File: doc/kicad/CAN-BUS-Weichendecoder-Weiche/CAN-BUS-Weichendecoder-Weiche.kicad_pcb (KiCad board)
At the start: 2 copper layers, 109.2 x 81.3 mm, 43 parts, among them J1 250-1404, J2 250-1404, J22 CAN-BUS, J23 CAN-BUS, J3 250-1404, J4 250-1404, J5 250-1404, J6 GND 12V DC +, J7 DCC IN, J8 I²C D C + -, U1 6N136, U2 Arduino_Nano, U3 ULN2803A, U4 ULN2803A, U5 TSR_1-2450

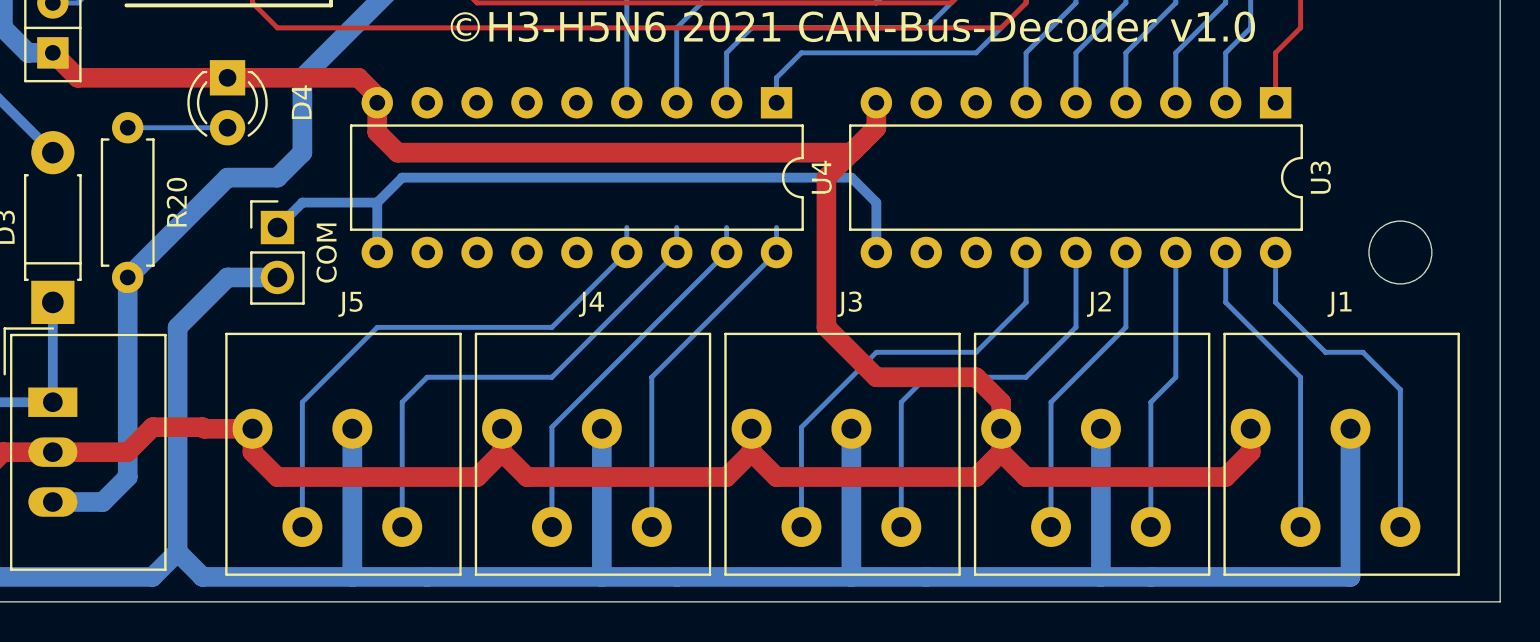
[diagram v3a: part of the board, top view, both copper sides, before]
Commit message: Buchen zu den Weichen gedreht, damit sie besser auf das Board passsen
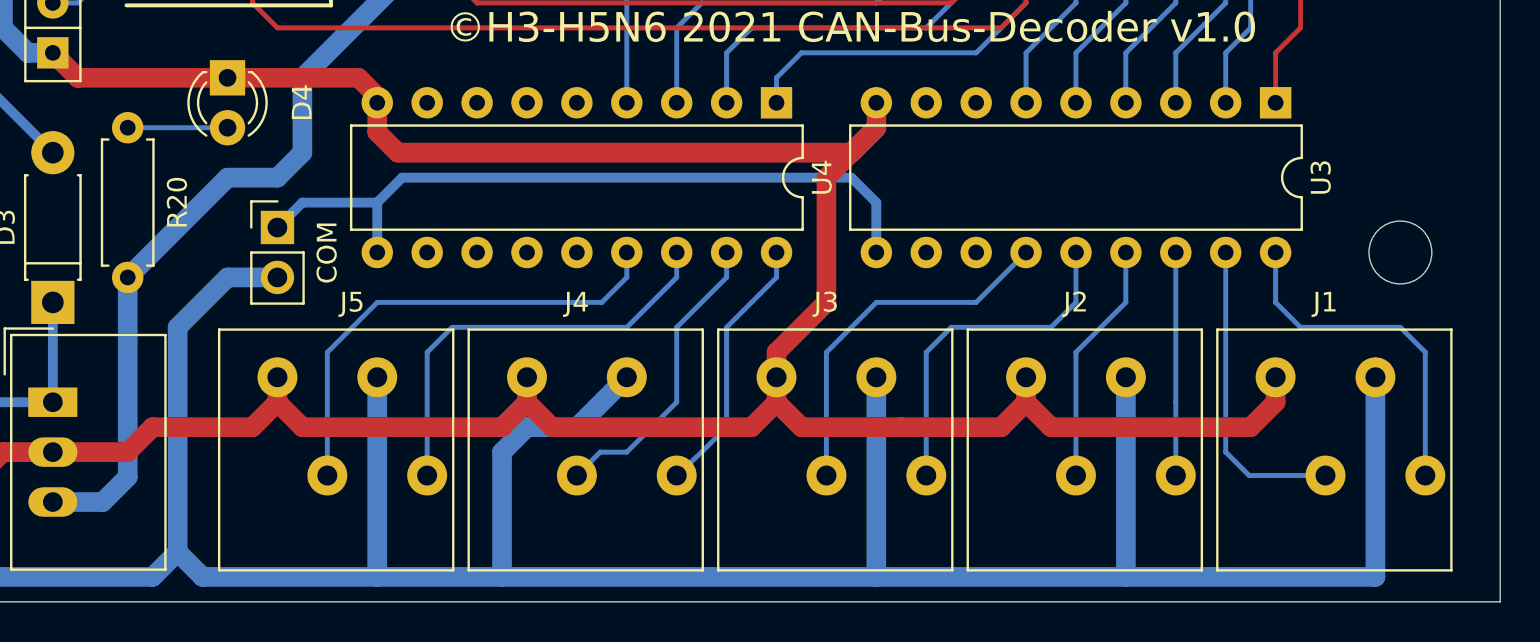
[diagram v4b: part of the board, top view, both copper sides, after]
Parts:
- moved J1 9.92 mm to (154.9, 91.4), turned to 0 degrees
- moved J2 9.92 mm to (142.2, 91.4), turned to 0 degrees
- moved J3 9.92 mm to (129.5, 91.4), turned to 0 degrees
- moved J4 9.92 mm to (116.8, 91.4), turned to 0 degrees
- moved J5 9.92 mm to (104.1, 91.4), turned to 0 degrees
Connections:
- J1 pad 1: Net-(J1-Pad1) -> GND
- J1 pad 2: +12V -> Net-(J1-Pad2)
- J1 pad 3: Net-(J1-Pad3) -> +12V
- J1 pad 4: GND -> Net-(J1-Pad4)
- J2 pad 1: Net-(J2-Pad1) -> GND
- J2 pad 2: +12V -> Net-(J2-Pad2)
- J2 pad 3: Net-(J2-Pad3) -> +12V
- J2 pad 4: GND -> Net-(J2-Pad4)
- J3 pad 1: Net-(J3-Pad1) -> GND
- J3 pad 2: +12V -> Net-(J3-Pad2)
- J3 pad 3: Net-(J3-Pad3) -> +12V
- J3 pad 4: GND -> Net-(J3-Pad4)
- J4 pad 1: Net-(J4-Pad1) -> GND
- J4 pad 2: +12V -> Net-(J4-Pad2)
- J4 pad 3: Net-(J4-Pad3) -> +12V
- J4 pad 4: GND -> Net-(J4-Pad4)
- J5 pad 1: Net-(J5-Pad1) -> GND
- J5 pad 2: +12V -> Net-(J5-Pad2)
- J5 pad 3: Net-(J5-Pad3) -> +12V
- J5 pad 4: GND -> Net-(J5-Pad4)
- U3 pad 13: Net-(J3-Pad3) -> Net-(J3-Pad2)
- U3 pad 14: Net-(J3-Pad1) -> Net-(J3-Pad4)
- U3 pad 15: Net-(J2-Pad3) -> Net-(J2-Pad2)
- U3 pad 16: Net-(J2-Pad1) -> Net-(J2-Pad4)
- U3 pad 17: Net-(J1-Pad3) -> Net-(J1-Pad2)
- U3 pad 18: Net-(J1-Pad1) -> Net-(J1-Pad4)
- U4 pad 15: Net-(J5-Pad3) -> Net-(J5-Pad2)
- U4 pad 16: Net-(J5-Pad1) -> Net-(J5-Pad4)
- U4 pad 17: Net-(J4-Pad3) -> Net-(J4-Pad2)
- U4 pad 18: Net-(J4-Pad1) -> Net-(J4-Pad4)
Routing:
- net Net-(J5-Pad3): track 27.3 -> 0.00 mm
- net Net-(J5-Pad1): track 24.7 -> 0.00 mm
- net Net-(J5-Pad2): track 0.00 -> 24.4 mm
- net Net-(J5-Pad4): track 0.00 -> 21.9 mm
- net Net-(J3-Pad3): track 21.7 -> 0.00 mm
- net Net-(J3-Pad1): track 20.6 -> 0.00 mm
- net Net-(J4-Pad3): track 18.9 -> 0.00 mm
- net Net-(J3-Pad2): track 0.00 -> 18.5 mm
- net +12V: track 153.0 -> 171.5 mm
- net Net-(J4-Pad1): track 18.0 -> 0.00 mm
- net Net-(J1-Pad1): track 17.7 -> 0.00 mm
- net Net-(J3-Pad4): track 0.00 -> 17.6 mm
- net Net-(J1-Pad4): track 0.00 -> 17.5 mm
- net Net-(J1-Pad2): track 0.00 -> 15.7 mm
- net Net-(J2-Pad3): track 15.5 -> 0.00 mm
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
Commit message: Aufgeräumt
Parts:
- added C1: 22µ/16V, Capacitors_THT:CP_Radial_D4.0mm_P1.50mm, F.Cu at (96.3, 113.0)
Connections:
- U3 pad 1: Net-(DS1-Pad8) -> Net-(DS1-Pad10)
- U3 pad 2: Net-(DS1-Pad7) -> Net-(DS1-Pad9)
- U3 pad 3: Net-(DS1-Pad6) -> Net-(DS1-Pad8)
- U3 pad 4: Net-(DS1-Pad5) -> Net-(DS1-Pad7)
- U3 pad 5: Net-(DS1-Pad4) -> Net-(DS1-Pad6)
- U3 pad 6: Net-(DS1-Pad3) -> Net-(DS1-Pad5)
- U4 pad 1: Net-(DS1-Pad2) -> Net-(DS1-Pad4)
- U4 pad 2: Net-(DS1-Pad1) -> Net-(DS1-Pad3)
- U4 pad 3: Net-(DS1-Pad9) -> Net-(DS1-Pad2)
- U4 pad 4: Net-(DS1-Pad10) -> Net-(DS1-Pad1)
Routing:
- net Net-(DS1-Pad7): track 78.9 -> 93.7 mm
- net Net-(DS1-Pad9): track 89.0 -> 74.1 mm, vias 0 -> 1
- net Net-(DS1-Pad2): track 66.7 -> 52.4 mm
- net Net-(DS1-Pad3): track 50.4 -> 64.1 mm
- net Net-(DS1-Pad1): track 54.7 -> 41.7 mm, vias 0 -> 1
- net Net-(DS1-Pad4): track 54.7 -> 67.0 mm
- net Net-(DS1-Pad8): track 75.1 -> 85.9 mm
- net Net-(DS1-Pad6): track 63.4 -> 67.0 mm
- net Net-(DS1-Pad5): track 59.0 -> 62.6 mm
- net Net-(DS1-Pad10): track 70.4 -> 73.4 mm
- net Net-(Shield1-Pad7): track 56.5 -> 58.0 mm
- net Net-(D1-Pad2): track 60.0 -> 61.5 mm
- net Net-(Shield1-Pad5): track 41.3 -> 40.2 mm
- net Net-(R2-Pad2): track 91.7 -> 90.7 mm
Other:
- net class Default removed
- net class Power removed
